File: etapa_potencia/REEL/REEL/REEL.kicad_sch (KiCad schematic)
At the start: 24 parts, among them J1 Conn_display2, J2 Conn_display_2, J3 Conn_teclado, J4 Conn_audio, J6 Salida_amp, J7 Entrada_buzzer, SW1 SW_Push, SW3 SW_Push, SW4 BW, SW5 FW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

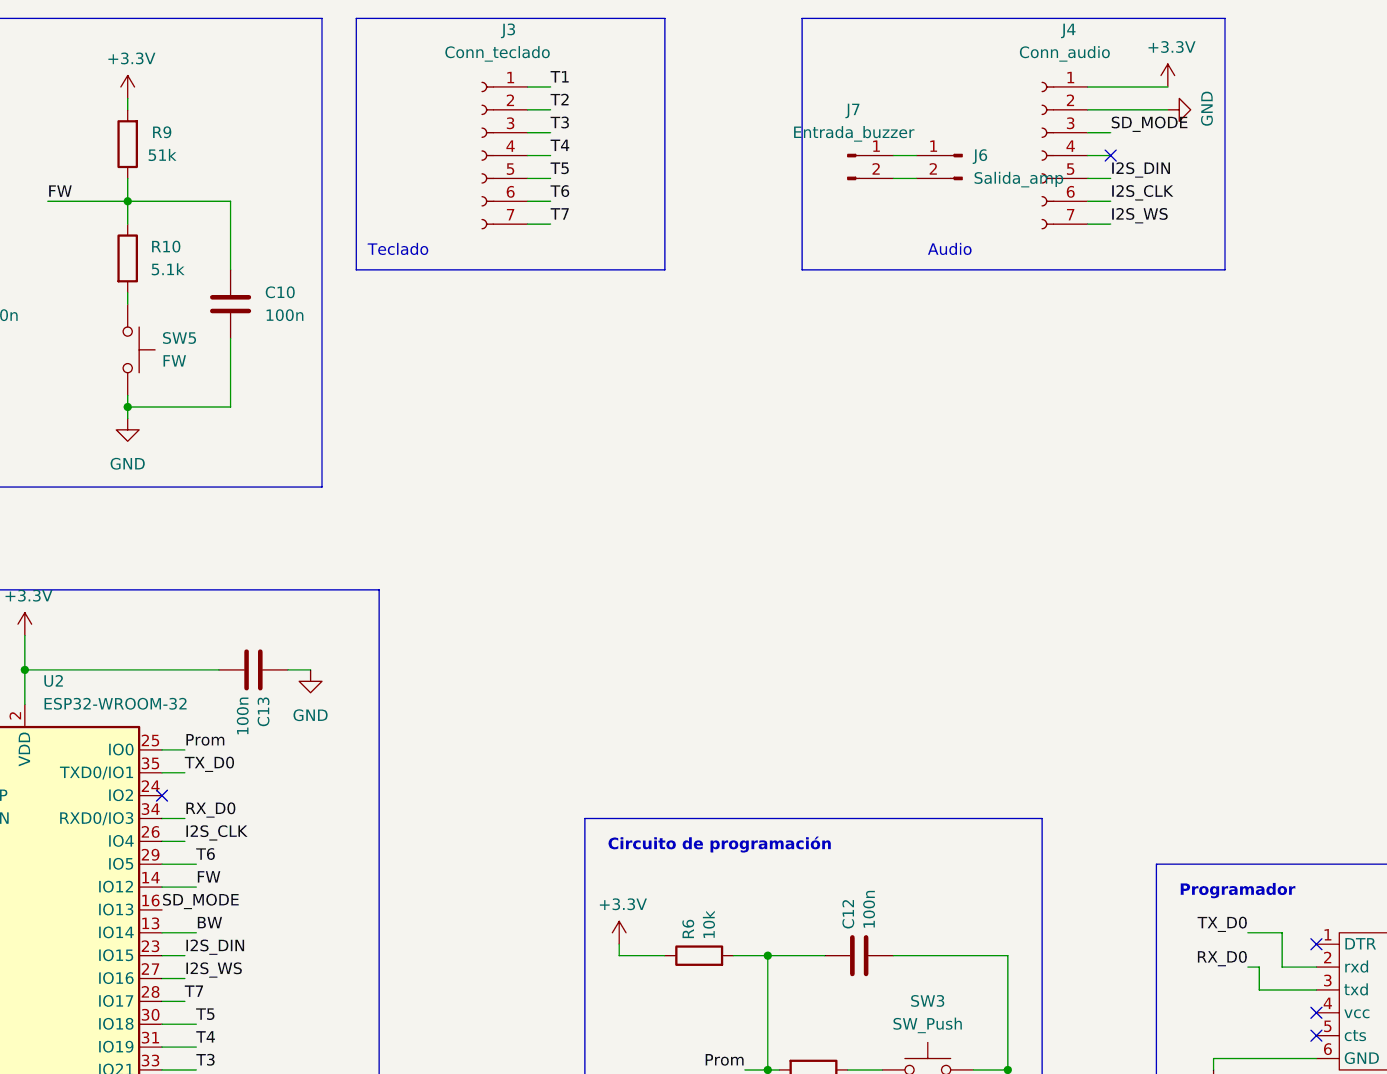
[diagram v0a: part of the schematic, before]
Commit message: Cambio orden pines etapa de audio
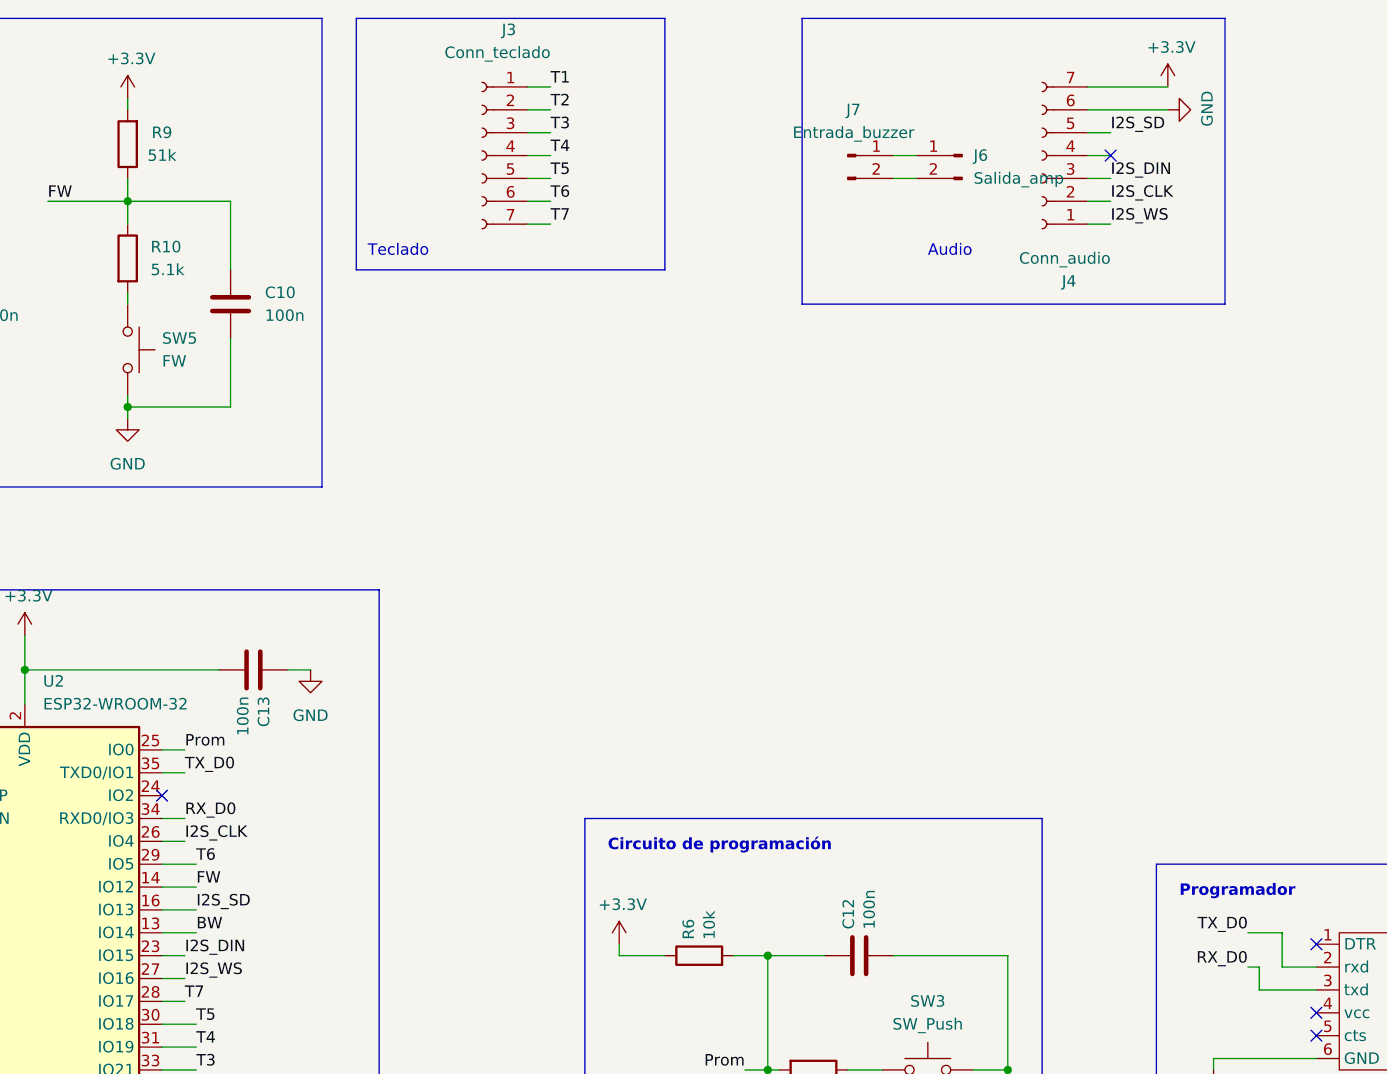
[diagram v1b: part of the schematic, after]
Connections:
- net +3V3: now also J4.7 (Pin_7); no longer J4.1 (Pin_1)
- net GND: now also J4.6 (Pin_6); no longer J4.2 (Pin_2)
- net I2S_CLK: now also J4.2 (Pin_2); no longer J4.6 (Pin_6)
- net I2S_DIN: now also J4.3 (Pin_3); no longer J4.5 (Pin_5)
- net I2S_WS: now also J4.1 (Pin_1); no longer J4.7 (Pin_7)
- net SD_MODE renamed I2S_SD
- net I2S_SD: now also J4.5 (Pin_5); no longer J4.3 (Pin_3)
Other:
- moved on the sheet: J4
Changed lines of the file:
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@@
     (stroke (width 0) (type default) (color 0 0 0 0))
   )
-  (polyline (pts (xy 200.66 54.61) (xy 200.66 26.67))
+  (polyline (pts (xy 200.66 58.42) (xy 200.66 26.67))
     (stroke (width 0) (type default) (color 0 0 0 0))
   )
@@
     (stroke (width 0) (type default) (color 0 0 0 0))
   )
-  (polyline (pts (xy 247.65 26.67) (xy 247.65 54.61))
+  (polyline (pts (xy 247.65 26.67) (xy 247.65 58.42))
+    (stroke (width 0) (type default) (color 0 0 0 0))
+  )
+  (wire (pts (xy 133.35 125.73) (xy 129.54 125.73))
     (stroke (width 0) (type default) (color 0 0 0 0))
   )
@@
     (stroke (width 0) (type default) (color 0 0 0 0))
   )
-  (polyline (pts (xy 247.65 54.61) (xy 200.66 54.61))
+  (polyline (pts (xy 247.65 58.42) (xy 200.66 58.42))
     (stroke (width 0) (type default) (color 0 0 0 0))
   )
@@
     (effects (font (size 1.27 1.27)) (justify left bottom))
   )
-  (label "SD_MODE" (at 234.95 39.37 0)
+  (label "I2S_SD" (at 234.95 39.37 0)
     (effects (font (size 1.27 1.27)) (justify left bottom))
   )
@@
     (effects (font (size 1.27 1.27)) (justify left bottom))
   )
-  (label "SD_MODE" (at 129.54 125.73 0)
+  (label "I2S_SD" (at 133.35 125.73 0)
     (effects (font (size 1.27 1.27)) (justify left bottom))
   )
@@
     (pin "1")
   )
-  (symbol (lib_id "Connector:Conn_01x07_Female") (at 227.33 41.91 0) (mirror y) (unit 1)
+  (symbol (lib_id "Connector:Conn_01x07_Female") (at 227.33 41.91 180) (unit 1)
     (in_bom yes) (on_board yes)
-    (property "Reference" "J4" (id 0) (at 231.14 27.94 0)
-      (effects (font (size 1.27 1.27)) (justify left))
-    )
-    (property "Value" "Conn_audio" (id 1) (at 234.95 30.48 0)
-      (effects (font (size 1.27 1.27)) (justify left))
-    )
+    (property "Reference" "J4" (id 0) (at 231.14 55.88 0)
+      (effects (font (size 1.27 1.27)) (justify left))
+    )
+    (property "Value" "Conn_audio" (id 1) (at 234.95 53.34 0)
+      (effects (font (size 1.27 1.27)) (justify left))
+    )

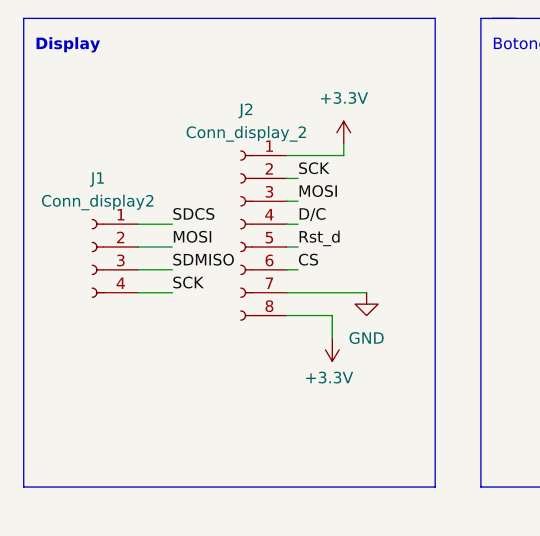
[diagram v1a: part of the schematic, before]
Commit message: Adición conector de tarjeta SD
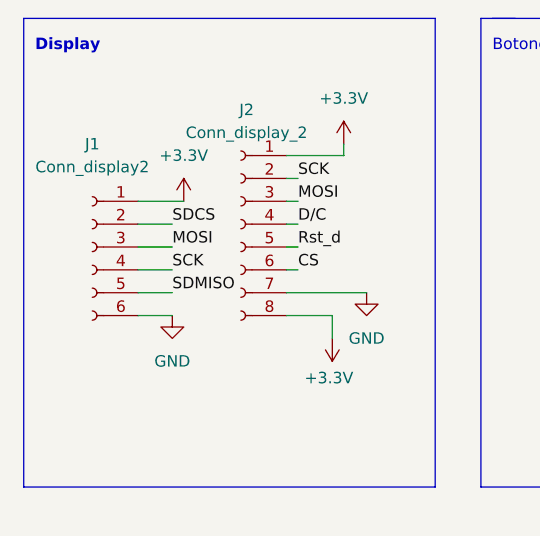
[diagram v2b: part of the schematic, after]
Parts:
- J1: footprint Connector_JST:JST_EH_B4B-EH-A_1x04_P2.50mm_Vertical -> (none); symbol Connector:Conn_01x04_Female -> Connector:Conn_01x06_Female
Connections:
- net +3V3: now also J1.1 (Pin_1)
- net GND: now also J1.6 (Pin_6)
- net MOSI: now also J1.3 (Pin_3); no longer J1.2 (Pin_2)
- net SDCS: now also J1.2 (Pin_2); no longer J1.1 (Pin_1)
- net SDMISO: now also J1.5 (Pin_5); no longer J1.3 (Pin_3)

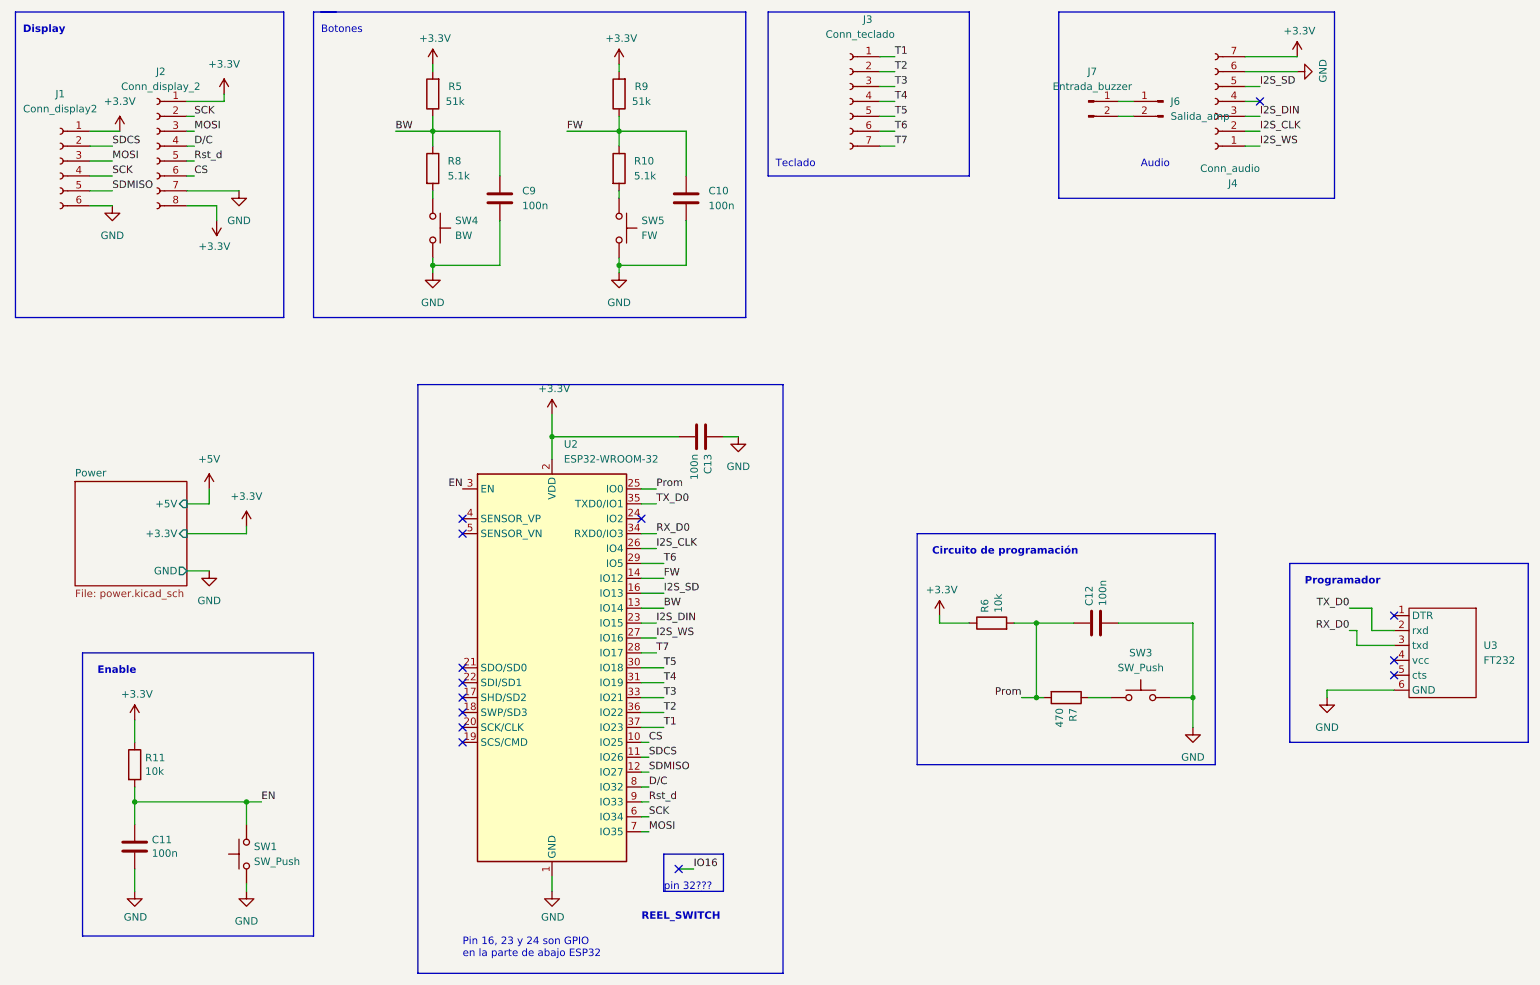
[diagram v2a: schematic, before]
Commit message: Últimos arreglos PCB
Resistencias de pull down de teclado y pin MISO de la sd, pin 12 queda libre, pines 34 y 35 quedan de entrada únicamente.
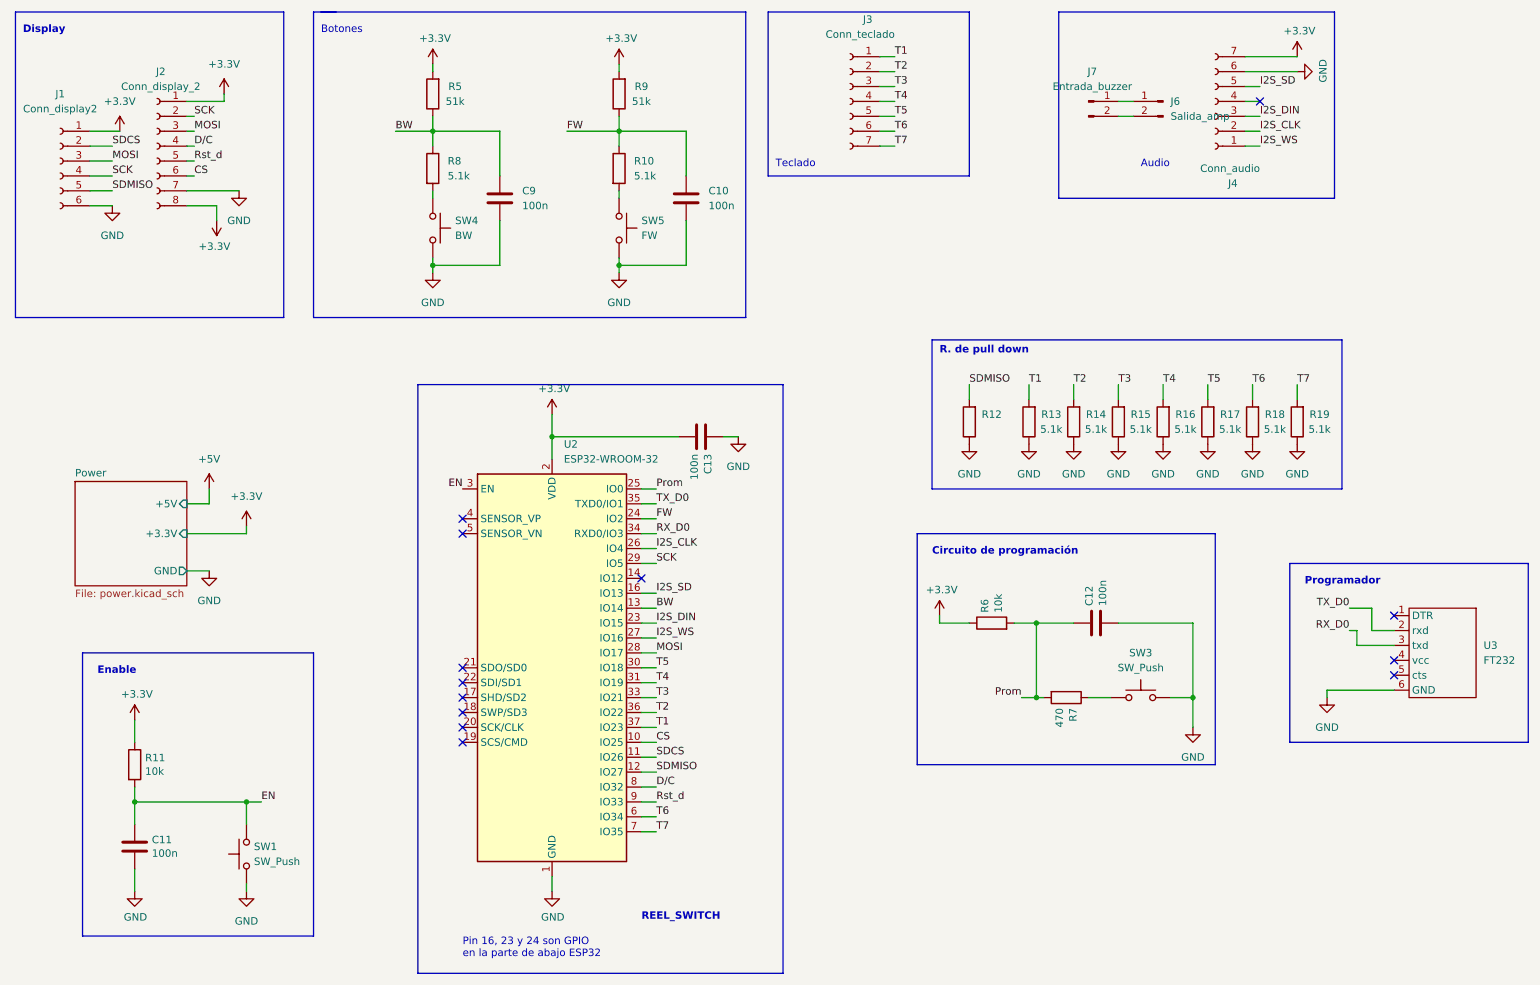
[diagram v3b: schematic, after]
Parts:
- added R12: (no value), Resistor_SMD:R_0805_2012Metric_Pad1.20x1.40mm_HandSolder, symbol Device:R
- added R13, R14, R15, R16, R17, R18, R19: 5.1k, Resistor_SMD:R_0805_2012Metric_Pad1.20x1.40mm_HandSolder, symbol Device:R
- J1: footprint (none) -> Connector_PinHeader_2.54mm:PinHeader_1x06_P2.54mm_Vertical
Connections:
- net FW: now also U2.24 (IO2); no longer U2.14 (IO12)
- net GND: now also R12.1, R13.1, R14.1, R15.1, R16.1, R17.1, R18.1, R19.1
- net MOSI: now also U2.28 (IO17); no longer U2.7 (IO35)
- net SCK: now also U2.29 (IO5); no longer U2.6 (IO34)
- net SDMISO: now also R12.2
- net T1: now also R13.2
- net T2: now also R14.2
- net T3: now also R15.2
- net T4: now also R16.2
- net T5: now also R17.2
- net T6: now also U2.6 (IO34), R18.2; no longer U2.29 (IO5)
- net T7: now also U2.7 (IO35), R19.2; no longer U2.28 (IO17)
- no-connect marks 14 -> 13
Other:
- note added: "R. de pull down"
- note removed: "pin 32???"
